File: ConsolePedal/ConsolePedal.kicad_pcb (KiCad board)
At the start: 2 copper layers, 86.4 x 77.5 mm, 13 parts, among them J1 AudioJack3, J2 AudioJack2, J3 Conn_02x25_Odd_Even

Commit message: Added n64 logo and regenerated gerber files
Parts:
- removed the G*** at (142.2, 58.4)
- removed the G*** at (133.3, 58.4)
- added G***: LOGO, libraries:n64Logo, F.Cu at (137.2, 61.0)
- added G***: LOGO, libraries:n64Logo, B.Cu at (137.2, 61.0)

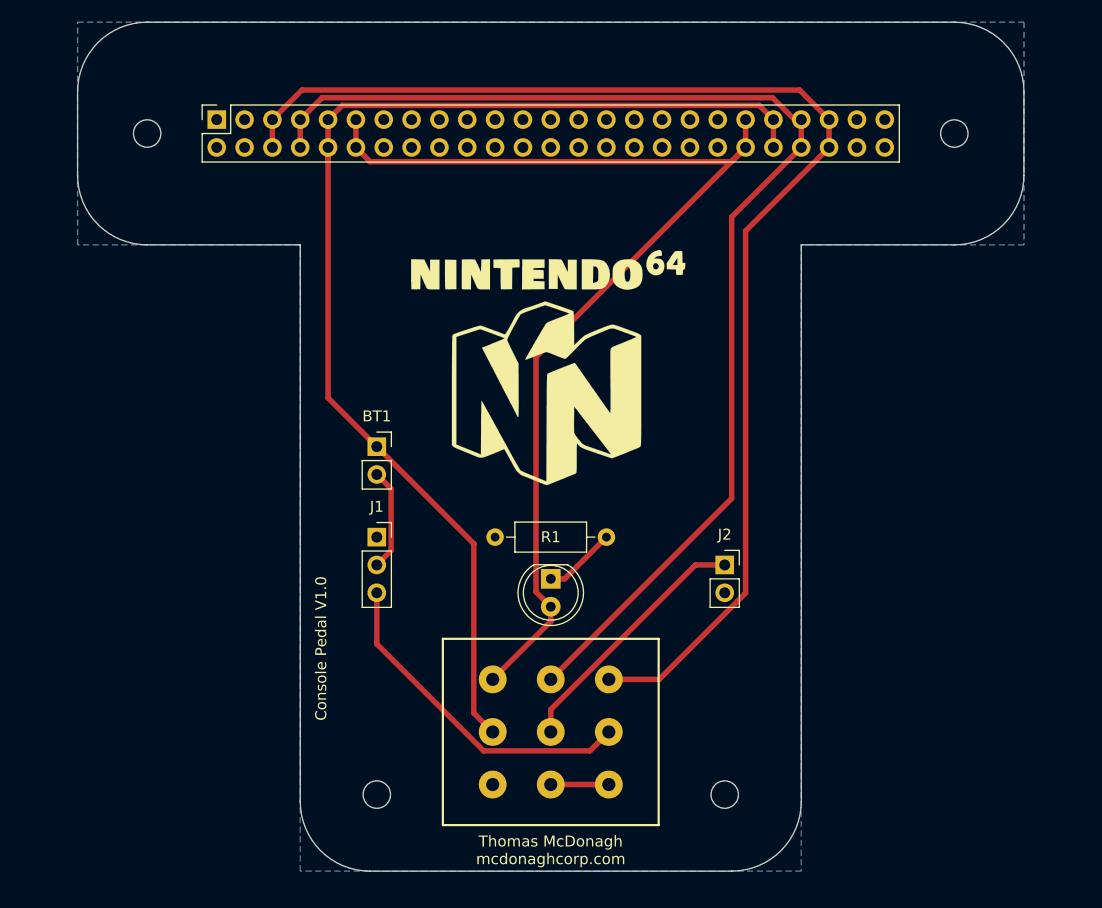
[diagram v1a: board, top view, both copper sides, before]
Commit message: Switched from SMT to THT since component count is low. Boards finalized and order completed based on this version.
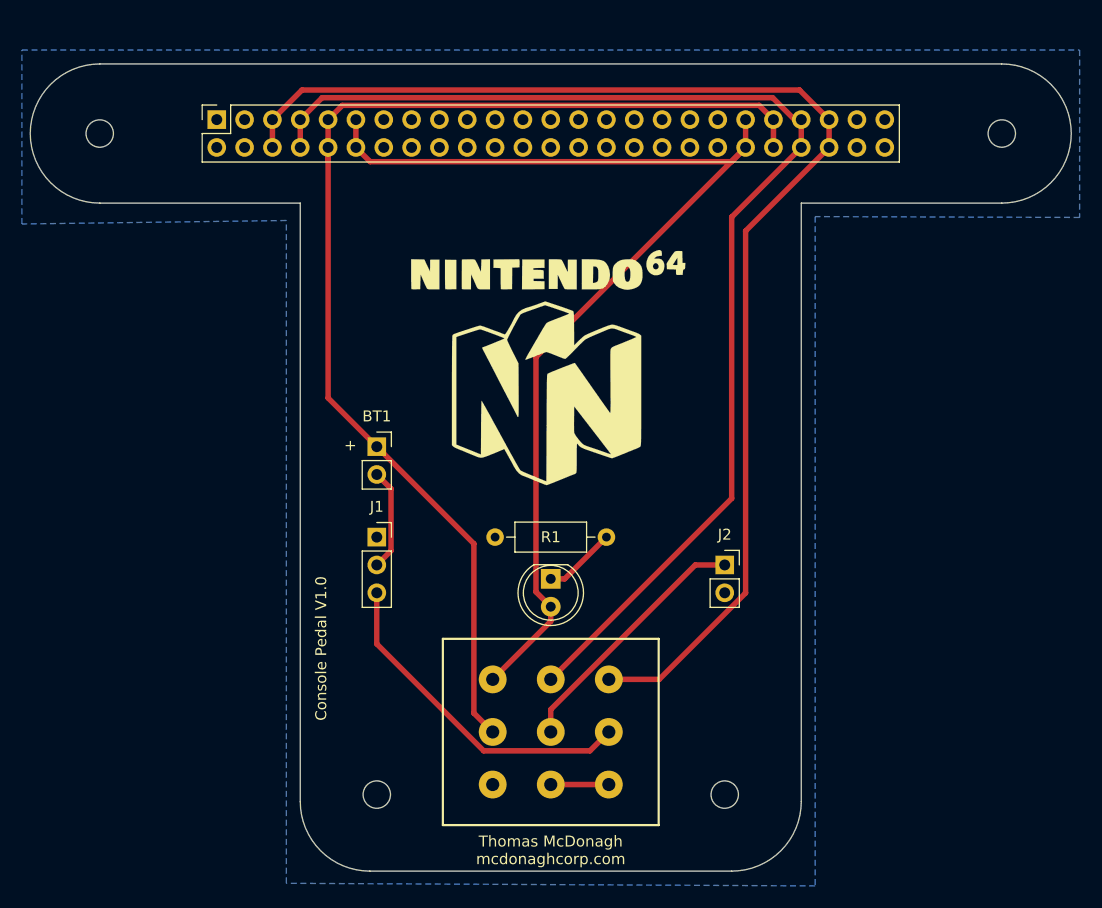
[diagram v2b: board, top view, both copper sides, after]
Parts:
- moved REF** 4.33 mm to (96.0, 39.4)
- moved REF** 4.33 mm to (178.3, 39.4)
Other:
- board size 86.4 x 77.5 mm -> 95 x 73.7 mm
- board text added: "+"
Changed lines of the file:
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@@
   (general
     (thickness 1.6)
-    (drawings 18)
+    (drawings 15)
     (tracks 52)
     (zones 0)
@@
   (page A4)
   (layers
-    (0 F.Cu signal)
+    (0 F.Cu signal hide)
     (31 B.Cu signal hide)
     (32 B.Adhes user)
@@
     (mod_text_size 1 1)
     (mod_text_width 0.15)
-    (pad_size 1.524 1.524)
-    (pad_drill 0.762)
+    (pad_size 2.5 2.5)
+    (pad_drill 2.5)
     (pad_to_mask_clearance 0)
     (aux_axis_origin 0 0)
@@
   )
   (module MountingHole:MountingHole_2.5mm (layer F.Cu)
-    (at 100.33 39.37)
+    (at 96 39.37)
     (descr "Mounting Hole 2.5mm, no annular")
     (tags "mounting hole 2.5mm no annular")
@@
   )
   (module MountingHole:MountingHole_2.5mm (layer F.Cu)
-    (at 173.99 39.37)
+    (at 178.32 39.37)
     (descr "Mounting Hole 2.5mm, no annular")
     (tags "mounting hole 2.5mm no annular")
@@
     )
   )
+  (gr_line (start 178.308 33.02) (end 96.012 33.02) (layer Edge.Cuts) (width 0.05))
+  (gr_line (start 160.02 45.72) (end 178.308 45.72) (layer Edge.Cuts) (width 0.05))
+  (gr_line (start 96.012 45.72) (end 114.3 45.72) (layer Edge.Cuts) (width 0.05))
+  (gr_line (start 160.02 45.72) (end 160.02 100.33) (layer Edge.Cuts) (width 0.05))
+  (gr_line (start 114.3 45.72) (end 114.3 100.33) (layer Edge.Cuts) (width 0.05))
+  (gr_arc (start 96.012 39.37) (end 96.012 33.02) (angle -180) (layer Edge.Cuts) (width 0.05))
+  (gr_arc (start 178.308 39.37) (end 178.308 45.72) (angle -180) (layer Edge.Cuts) (width 0.05))
+  (gr_text + (at 118.872 67.818) (layer F.SilkS)
+    (effects (font (size 1 1) (thickness 0.15)))
+  )
   (gr_text "Console Pedal V1.0" (at 116.205 86.36 90) (layer B.SilkS)
     (effects (font (size 1 1) (thickness 0.25)) (justify mirror))
@@
     (effects (font (size 1 1) (thickness 0.25)))
   )
-  (gr_line (start 114.3 49.53) (end 100.33 49.53) (layer Edge.Cuts) (width 0.05))
-  (gr_line (start 114.3 100.33) (end 114.3 49.53) (layer Edge.Cuts) (width 0.05))
-  (gr_line (start 160.02 49.53) (end 173.99 49.53) (layer Edge.Cuts) (width 0.05))
-  (gr_line (start 160.02 100.33) (end 160.02 49.53) (layer Edge.Cuts) (width 0.05))
   (gr_line (start 120.65 106.68) (end 153.67 106.68) (layer Edge.Cuts) (width 0.05))
   (gr_arc (start 153.67 100.33) (end 153.67 106.68) (angle -90) (layer Edge.Cuts) (width 0.05))
   (gr_arc (start 120.65 100.33) (end 114.3 100.33) (angle -90) (layer Edge.Cuts) (width 0.05))
-  (gr_line (start 180.34 35.56) (end 180.34 43.18) (layer Edge.Cuts) (width 0.05))
-  (gr_line (start 100.33 29.21) (end 173.99 29.21) (layer Edge.Cuts) (width 0.05))
-  (gr_arc (start 173.99 43.18) (end 173.99 49.53) (angle -90) (layer Edge.Cuts) (width 0.05))
-  (gr_line (start 93.98 35.56) (end 93.98 43.18) (layer Edge.Cuts) (width 0.05))
-  (gr_arc (start 100.33 43.18) (end 93.98 43.18) (angle -90) (layer Edge.Cuts) (width 0.05))
-  (gr_arc (start 100.33 35.56) (end 100.33 29.21) (angle -90) (layer Edge.Cuts) (width 0.05))
-  (gr_arc (start 173.99 35.56) (end 180.34 35.56) (angle -90) (layer Edge.Cuts) (width 0.05))
   (segment (start 122.585001 71.785001) (end 121.285 70.485) (width 0.5) (layer F.Cu) (net 1))
   (segment (start 122.585001 77.439999) (end 122.585001 71.785001) (width 0.5) (layer F.Cu) (net 1))
@@
     (polygon
       (pts
-        (xy 180.34 49.53) (xy 160.02 49.53) (xy 160.02 106.68) (xy 114.3 106.68) (xy 114.3 49.53)
-        (xy 93.98 49.53) (xy 93.98 29.21) (xy 180.34 29.21)
+        (xy 185.42 47.029688) (xy 161.29 46.950313) (xy 161.29 108.029375) (xy 113.03 107.79125) (xy 113.03 47.3075)
+        (xy 88.9 47.625) (xy 88.9 31.75) (xy 185.42 31.75)
       )
     )

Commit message: Made n64 connector pins further apart to match real socket connector and moved led for easier mounting
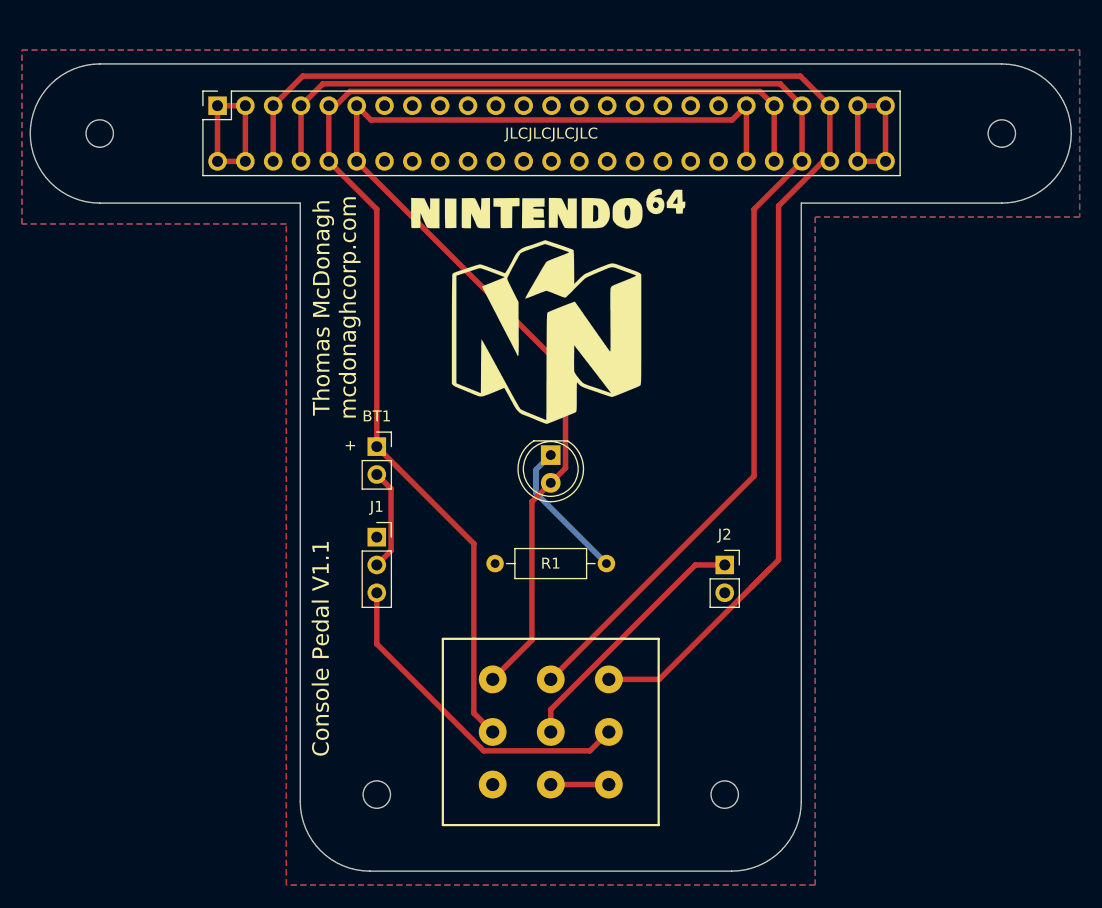
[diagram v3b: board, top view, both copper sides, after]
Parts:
- J3: footprint Connector_PinSocket_2.54mm:PinSocket_2x25_P2.54mm_Vertical -> libraries:n64Socket
- moved D1 11.3 mm to (137.2, 68.7)
- moved G*** 5.59 mm to (137.2, 55.4) (x2)
- moved R1 2.41 mm to (142.2, 78.6)
- moved J3 1.27 mm to (106.8, 36.8)
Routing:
- net GND: track 0.00 -> 30.5 mm
- net Net-(D1-Pad1): track 6.66 -> 13.1 mm
- net /Input: track 117.7 -> 124.1 mm
- net /LEDPower: track 100.9 -> 105.4 mm
- net /Output: track 111.3 -> 114.3 mm
- net +9V: track 107.6 -> 110.1 mm
- added copper zone on F.Cu, net GND
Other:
- board text added: "Console Pedal V1.1"
- board text added: "JLCJLCJLCJLC"
- board text removed: "Console Pedal V1.0"

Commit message: Moving polarity protection diode to mainboard so each cartridge doesn't need to have its own
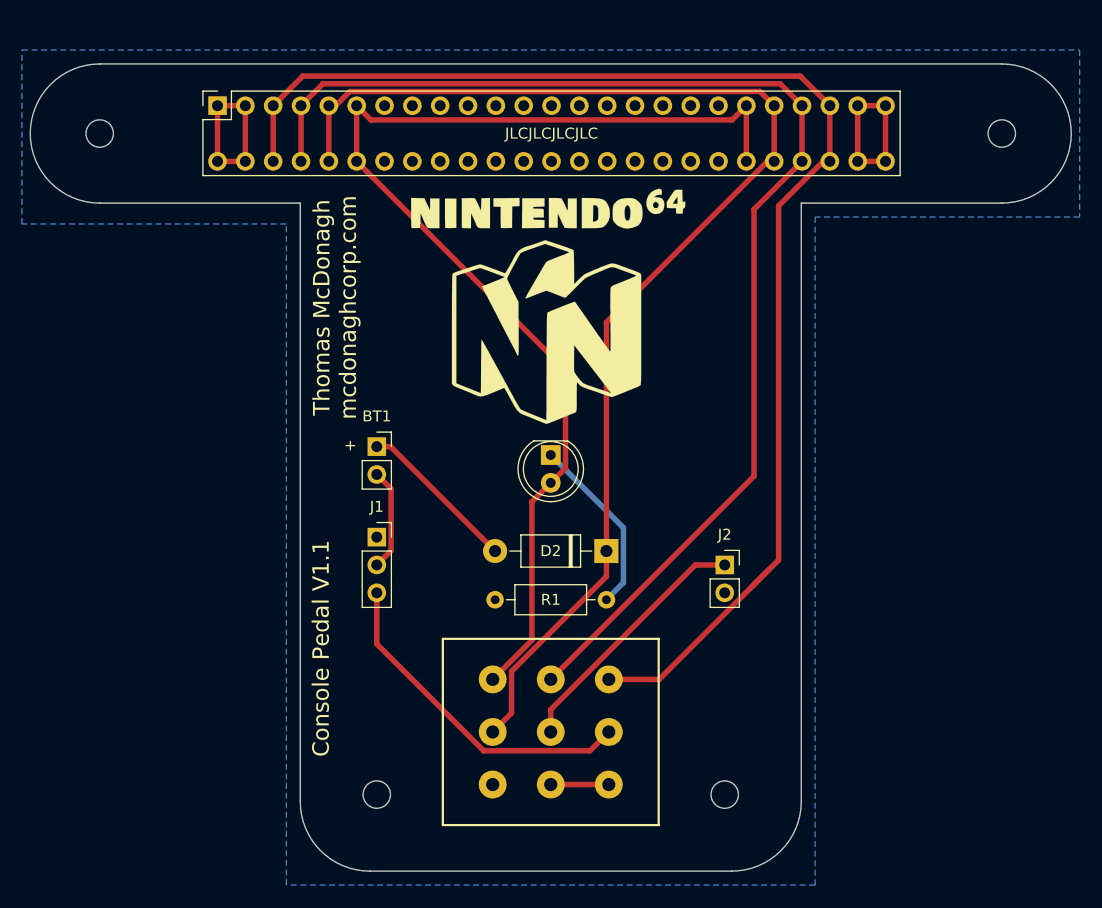
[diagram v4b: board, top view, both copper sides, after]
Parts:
- added D2: D, Diode_THT:D_DO-41_SOD81_P10.16mm_Horizontal, F.Cu at (142.2, 77.5)
- moved R1 3.30 mm to (142.2, 81.9)
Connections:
- BT1 pad 1: +9V -> Net-(BT1-Pad1)
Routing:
- net Net-(BT1-Pad1): track 0.00 -> 14.7 mm
- net +9V: track 110.1 -> 114.9 mm
- net Net-(D1-Pad1): track 13.1 -> 16.6 mm
- removed copper zone on F.Cu, net GND

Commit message: Fixed missing grounding plane
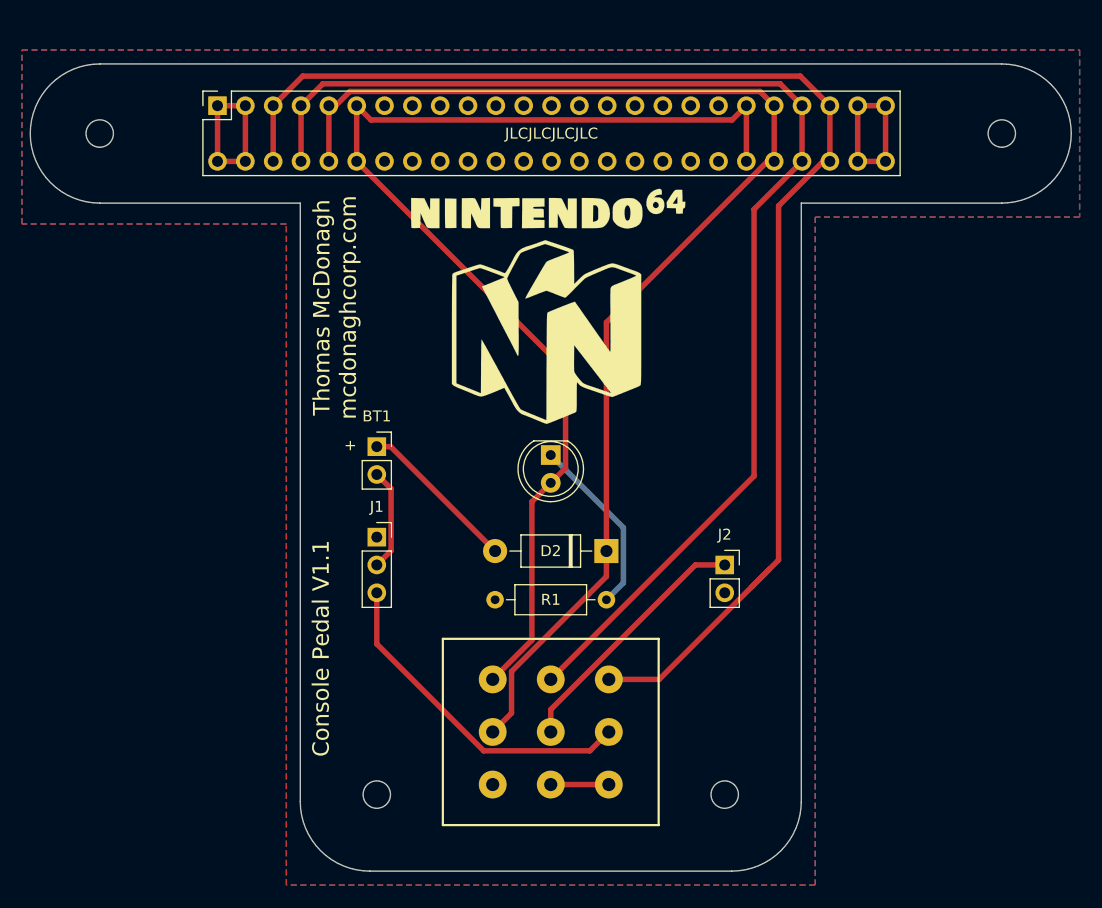
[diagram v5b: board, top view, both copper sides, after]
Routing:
- added copper zone on F.Cu, net GND
